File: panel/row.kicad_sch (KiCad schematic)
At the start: 16 parts

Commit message: Moving panel to subfolder
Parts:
- D? (x16): footprint ledcube:MHPA1515RGBDT -> panel:MHPA1515RGBDT
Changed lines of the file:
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@@
       (effects (font (size 1.27 1.27)) hide)
     )
-    (property "Footprint" "ledcube:MHPA1515RGBDT" (id 2) (at 114.3 58.42 0)
+    (property "Footprint" "panel:MHPA1515RGBDT" (id 2) (at 114.3 58.42 0)
       (effects (font (size 1.27 1.27)) hide)
     )
@@
       (effects (font (size 1.27 1.27)) hide)
     )
-    (property "Footprint" "ledcube:MHPA1515RGBDT" (id 2) (at 114.3 83.82 0)
+    (property "Footprint" "panel:MHPA1515RGBDT" (id 2) (at 114.3 83.82 0)
       (effects (font (size 1.27 1.27)) hide)
     )
@@
       (effects (font (size 1.27 1.27)) hide)
     )
-    (property "Footprint" "ledcube:MHPA1515RGBDT" (id 2) (at 114.3 109.22 0)
+    (property "Footprint" "panel:MHPA1515RGBDT" (id 2) (at 114.3 109.22 0)
       (effects (font (size 1.27 1.27)) hide)
     )
@@
       (effects (font (size 1.27 1.27)) hide)
     )
-    (property "Footprint" "ledcube:MHPA1515RGBDT" (id 2) (at 114.3 134.62 0)
+    (property "Footprint" "panel:MHPA1515RGBDT" (id 2) (at 114.3 134.62 0)
       (effects (font (size 1.27 1.27)) hide)
     )
@@
       (effects (font (size 1.27 1.27)) hide)
     )
-    (property "Footprint" "ledcube:MHPA1515RGBDT" (id 2) (at 135.89 58.42 0)
+    (property "Footprint" "panel:MHPA1515RGBDT" (id 2) (at 135.89 58.42 0)
       (effects (font (size 1.27 1.27)) hide)
     )
@@
       (effects (font (size 1.27 1.27)) hide)
     )
-    (property "Footprint" "ledcube:MHPA1515RGBDT" (id 2) (at 135.89 83.82 0)
+    (property "Footprint" "panel:MHPA1515RGBDT" (id 2) (at 135.89 83.82 0)
       (effects (font (size 1.27 1.27)) hide)
     )
@@
       (effects (font (size 1.27 1.27)) hide)
     )
-    (property "Footprint" "ledcube:MHPA1515RGBDT" (id 2) (at 135.89 109.22 0)
+    (property "Footprint" "panel:MHPA1515RGBDT" (id 2) (at 135.89 109.22 0)
       (effects (font (size 1.27 1.27)) hide)
     )
@@
       (effects (font (size 1.27 1.27)) hide)
     )
-    (property "Footprint" "ledcube:MHPA1515RGBDT" (id 2) (at 135.89 134.62 0)
+    (property "Footprint" "panel:MHPA1515RGBDT" (id 2) (at 135.89 134.62 0)
       (effects (font (size 1.27 1.27)) hide)
     )
@@
       (effects (font (size 1.27 1.27)) hide)
     )
-    (property "Footprint" "ledcube:MHPA1515RGBDT" (id 2) (at 157.48 58.42 0)
+    (property "Footprint" "panel:MHPA1515RGBDT" (id 2) (at 157.48 58.42 0)
       (effects (font (size 1.27 1.27)) hide)
     )
@@
       (effects (font (size 1.27 1.27)) hide)
     )
-    (property "Footprint" "ledcube:MHPA1515RGBDT" (id 2) (at 157.48 83.82 0)
+    (property "Footprint" "panel:MHPA1515RGBDT" (id 2) (at 157.48 83.82 0)
       (effects (font (size 1.27 1.27)) hide)
     )
@@
       (effects (font (size 1.27 1.27)) hide)
     )
-    (property "Footprint" "ledcube:MHPA1515RGBDT" (id 2) (at 157.48 109.22 0)
+    (property "Footprint" "panel:MHPA1515RGBDT" (id 2) (at 157.48 109.22 0)
       (effects (font (size 1.27 1.27)) hide)
     )
@@
       (effects (font (size 1.27 1.27)) hide)
     )
-    (property "Footprint" "ledcube:MHPA1515RGBDT" (id 2) (at 157.48 134.62 0)
+    (property "Footprint" "panel:MHPA1515RGBDT" (id 2) (at 157.48 134.62 0)
       (effects (font (size 1.27 1.27)) hide)
     )
@@
       (effects (font (size 1.27 1.27)) hide)
     )
-    (property "Footprint" "ledcube:MHPA1515RGBDT" (id 2) (at 179.07 58.42 0)
+    (property "Footprint" "panel:MHPA1515RGBDT" (id 2) (at 179.07 58.42 0)
       (effects (font (size 1.27 1.27)) hide)
     )
@@
       (effects (font (size 1.27 1.27)) hide)
     )
-    (property "Footprint" "ledcube:MHPA1515RGBDT" (id 2) (at 179.07 83.82 0)
+    (property "Footprint" "panel:MHPA1515RGBDT" (id 2) (at 179.07 83.82 0)
       (effects (font (size 1.27 1.27)) hide)
     )
@@
       (effects (font (size 1.27 1.27)) hide)
     )
-    (property "Footprint" "ledcube:MHPA1515RGBDT" (id 2) (at 179.07 109.22 0)
+    (property "Footprint" "panel:MHPA1515RGBDT" (id 2) (at 179.07 109.22 0)
       (effects (font (size 1.27 1.27)) hide)
     )
@@
       (effects (font (size 1.27 1.27)) hide)
     )
-    (property "Footprint" "ledcube:MHPA1515RGBDT" (id 2) (at 179.07 134.62 0)
-      (effects (font (size 1.27 1.27)) hide)
-    )
+    (property "Footprint" "panel:MHPA1515RGBDT" (id 2) (at 179.07 134.62 0)
+      (effects (font (size 1.27 1.27)) hide)
+    )

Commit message: Annotated schematic
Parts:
- removed D? (x15): LED_RABG, panel:MHPA1515RGBDT, symbol Device:LED_RABG
- added D242, D243, D244, D245, D246, D247, D248, D249, D250, D251, D252, D253, D254, D255, D256: LED_RABG, panel:MHPA1515RGBDT, symbol Device:LED_RABG
- gave numbers to parts that had none: 1
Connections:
- net COL_10B: now also D251.3 (BK)
- net COL_10G: now also D251.4 (GK)
- net COL_10R: now also D251.1 (RK)
- net COL_11B: now also D255.3 (BK)
- net COL_11G: now also D255.4 (GK)
- net COL_11R: now also D255.1 (RK)
- net COL_12B: now also D244.3 (BK)
- net COL_12G: now also D244.4 (GK)
- net COL_12R: now also D244.1 (RK)
- net COL_13B: now also D248.3 (BK)
- net COL_13G: now also D248.4 (GK)
- net COL_13R: now also D248.1 (RK)
- net COL_14B: now also D252.3 (BK)
- net COL_14G: now also D252.4 (GK)
- net COL_14R: now also D252.1 (RK)
- net COL_15B: now also D256.3 (BK)
- net COL_15G: now also D256.4 (GK)
- net COL_15R: now also D256.1 (RK)
- net COL_1B: now also D245.3 (BK)
- net COL_1G: now also D245.4 (GK)
- net COL_1R: now also D245.1 (RK)
- net COL_2B: now also D249.3 (BK)
- net COL_2G: now also D249.4 (GK)
- net COL_2R: now also D249.1 (RK)
- net COL_3B: now also D253.3 (BK)
- net COL_3G: now also D253.4 (GK)
- net COL_3R: now also D253.1 (RK)
- net COL_4B: now also D242.3 (BK)
- net COL_4G: now also D242.4 (GK)
- net COL_4R: now also D242.1 (RK)
- net COL_5B: now also D246.3 (BK)
- net COL_5G: now also D246.4 (GK)
- net COL_5R: now also D246.1 (RK)
- net COL_6B: now also D250.3 (BK)
- net COL_6G: now also D250.4 (GK)
- net COL_6R: now also D250.1 (RK)
- net COL_7B: now also D254.3 (BK)
- net COL_7G: now also D254.4 (GK)
- net COL_7R: now also D254.1 (RK)
- net COL_8B: now also D243.3 (BK)
- net COL_8G: now also D243.4 (GK)
- net COL_8R: now also D243.1 (RK)
- net COL_9B: now also D247.3 (BK)
- net COL_9G: now also D247.4 (GK)
- net COL_9R: now also D247.1 (RK)
- net COMMON: now also D242.2 (A), D243.2 (A), D244.2 (A), D245.2 (A), D246.2 (A), D247.2 (A), D248.2 (A), D249.2 (A), D250.2 (A), D251.2 (A), D252.2 (A), D253.2 (A), D254.2 (A), D255.2 (A), D256.2 (A)
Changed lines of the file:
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@@
   (symbol (lib_id "Device:LED_RABG") (at 113.03 58.42 90)
     (in_bom yes) (on_board yes)
-    (property "Reference" "D?" (id 0) (at 106.172 53.34 90))
+    (property "Reference" "D241" (id 0) (at 106.172 53.34 90))
     (property "Value" "LED_RABG" (id 1) (at 121.92 58.42 0)
       (effects (font (size 1.27 1.27)) hide)
@@
   (symbol (lib_id "Device:LED_RABG") (at 113.03 83.82 90)
     (in_bom yes) (on_board yes)
-    (property "Reference" "D?" (id 0) (at 106.172 78.74 90))
+    (property "Reference" "D242" (id 0) (at 106.172 78.74 90))
     (property "Value" "LED_RABG" (id 1) (at 121.92 83.82 0)
       (effects (font (size 1.27 1.27)) hide)
@@
   (symbol (lib_id "Device:LED_RABG") (at 113.03 109.22 90)
     (in_bom yes) (on_board yes)
-    (property "Reference" "D?" (id 0) (at 106.172 104.14 90))
+    (property "Reference" "D243" (id 0) (at 106.172 104.14 90))
     (property "Value" "LED_RABG" (id 1) (at 121.92 109.22 0)
       (effects (font (size 1.27 1.27)) hide)
@@
   (symbol (lib_id "Device:LED_RABG") (at 113.03 134.62 90)
     (in_bom yes) (on_board yes)
-    (property "Reference" "D?" (id 0) (at 106.172 129.54 90))
+    (property "Reference" "D244" (id 0) (at 106.172 129.54 90))
     (property "Value" "LED_RABG" (id 1) (at 121.92 134.62 0)
       (effects (font (size 1.27 1.27)) hide)
@@
   (symbol (lib_id "Device:LED_RABG") (at 134.62 58.42 90)
     (in_bom yes) (on_board yes)
-    (property "Reference" "D?" (id 0) (at 127.762 53.34 90))
+    (property "Reference" "D245" (id 0) (at 127.762 53.34 90))
     (property "Value" "LED_RABG" (id 1) (at 143.51 58.42 0)
       (effects (font (size 1.27 1.27)) hide)
@@
   (symbol (lib_id "Device:LED_RABG") (at 134.62 83.82 90)
     (in_bom yes) (on_board yes)
-    (property "Reference" "D?" (id 0) (at 127.762 78.74 90))
+    (property "Reference" "D246" (id 0) (at 127.762 78.74 90))
     (property "Value" "LED_RABG" (id 1) (at 143.51 83.82 0)
       (effects (font (size 1.27 1.27)) hide)
@@
   (symbol (lib_id "Device:LED_RABG") (at 134.62 109.22 90)
     (in_bom yes) (on_board yes)
-    (property "Reference" "D?" (id 0) (at 127.762 104.14 90))
+    (property "Reference" "D247" (id 0) (at 127.762 104.14 90))
     (property "Value" "LED_RABG" (id 1) (at 143.51 109.22 0)
       (effects (font (size 1.27 1.27)) hide)
@@
   (symbol (lib_id "Device:LED_RABG") (at 134.62 134.62 90)
     (in_bom yes) (on_board yes)
-    (property "Reference" "D?" (id 0) (at 127.762 129.54 90))
+    (property "Reference" "D248" (id 0) (at 127.762 129.54 90))
     (property "Value" "LED_RABG" (id 1) (at 143.51 134.62 0)
       (effects (font (size 1.27 1.27)) hide)
@@
   (symbol (lib_id "Device:LED_RABG") (at 156.21 58.42 90)
     (in_bom yes) (on_board yes)
-    (property "Reference" "D?" (id 0) (at 149.352 53.34 90))
+    (property "Reference" "D249" (id 0) (at 149.352 53.34 90))
     (property "Value" "LED_RABG" (id 1) (at 165.1 58.42 0)
       (effects (font (size 1.27 1.27)) hide)
@@
   (symbol (lib_id "Device:LED_RABG") (at 156.21 83.82 90)
     (in_bom yes) (on_board yes)
-    (property "Reference" "D?" (id 0) (at 149.352 78.74 90))
+    (property "Reference" "D250" (id 0) (at 149.352 78.74 90))
     (property "Value" "LED_RABG" (id 1) (at 165.1 83.82 0)
       (effects (font (size 1.27 1.27)) hide)
@@
   (symbol (lib_id "Device:LED_RABG") (at 156.21 109.22 90)
     (in_bom yes) (on_board yes)
-    (property "Reference" "D?" (id 0) (at 149.352 104.14 90))
+    (property "Reference" "D251" (id 0) (at 149.352 104.14 90))
     (property "Value" "LED_RABG" (id 1) (at 165.1 109.22 0)
       (effects (font (size 1.27 1.27)) hide)
@@
   (symbol (lib_id "Device:LED_RABG") (at 156.21 134.62 90)
     (in_bom yes) (on_board yes)
-    (property "Reference" "D?" (id 0) (at 149.352 129.54 90))
+    (property "Reference" "D252" (id 0) (at 149.352 129.54 90))
     (property "Value" "LED_RABG" (id 1) (at 165.1 134.62 0)
       (effects (font (size 1.27 1.27)) hide)
@@
   (symbol (lib_id "Device:LED_RABG") (at 177.8 58.42 90)
     (in_bom yes) (on_board yes)
-    (property "Reference" "D?" (id 0) (at 170.942 53.34 90))
+    (property "Reference" "D253" (id 0) (at 170.942 53.34 90))
     (property "Value" "LED_RABG" (id 1) (at 186.69 58.42 0)
       (effects (font (size 1.27 1.27)) hide)
@@
   (symbol (lib_id "Device:LED_RABG") (at 177.8 83.82 90)
     (in_bom yes) (on_board yes)
-    (property "Reference" "D?" (id 0) (at 170.942 78.74 90))
+    (property "Reference" "D254" (id 0) (at 170.942 78.74 90))
     (property "Value" "LED_RABG" (id 1) (at 186.69 83.82 0)
       (effects (font (size 1.27 1.27)) hide)
@@
   (symbol (lib_id "Device:LED_RABG") (at 177.8 109.22 90)
     (in_bom yes) (on_board yes)
-    (property "Reference" "D?" (id 0) (at 170.942 104.14 90))
+    (property "Reference" "D255" (id 0) (at 170.942 104.14 90))
     (property "Value" "LED_RABG" (id 1) (at 186.69 109.22 0)
       (effects (font (size 1.27 1.27)) hide)
@@
   (symbol (lib_id "Device:LED_RABG") (at 177.8 134.62 90)
     (in_bom yes) (on_board yes)
-    (property "Reference" "D?" (id 0) (at 170.942 129.54 90))
+    (property "Reference" "D256" (id 0) (at 170.942 129.54 90))
     (property "Value" "LED_RABG" (id 1) (at 186.69 134.62 0)
       (effects (font (size 1.27 1.27)) hide)

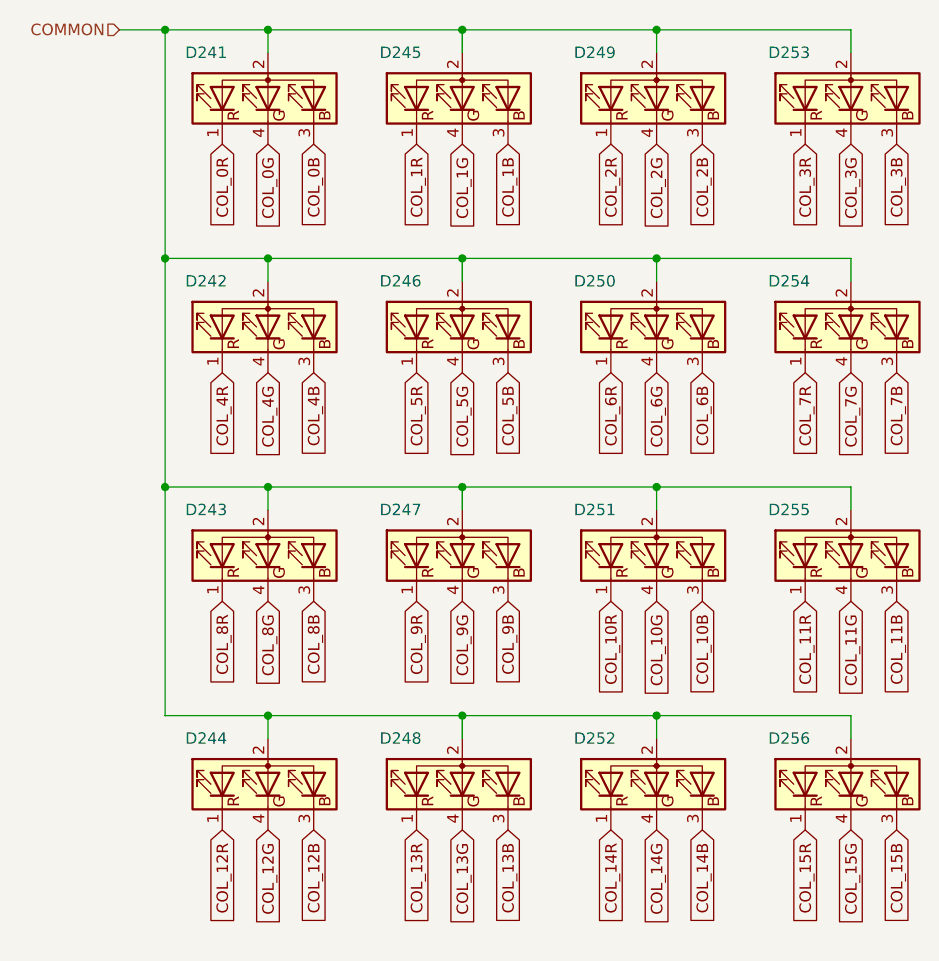
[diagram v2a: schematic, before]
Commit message: LED matrix placement
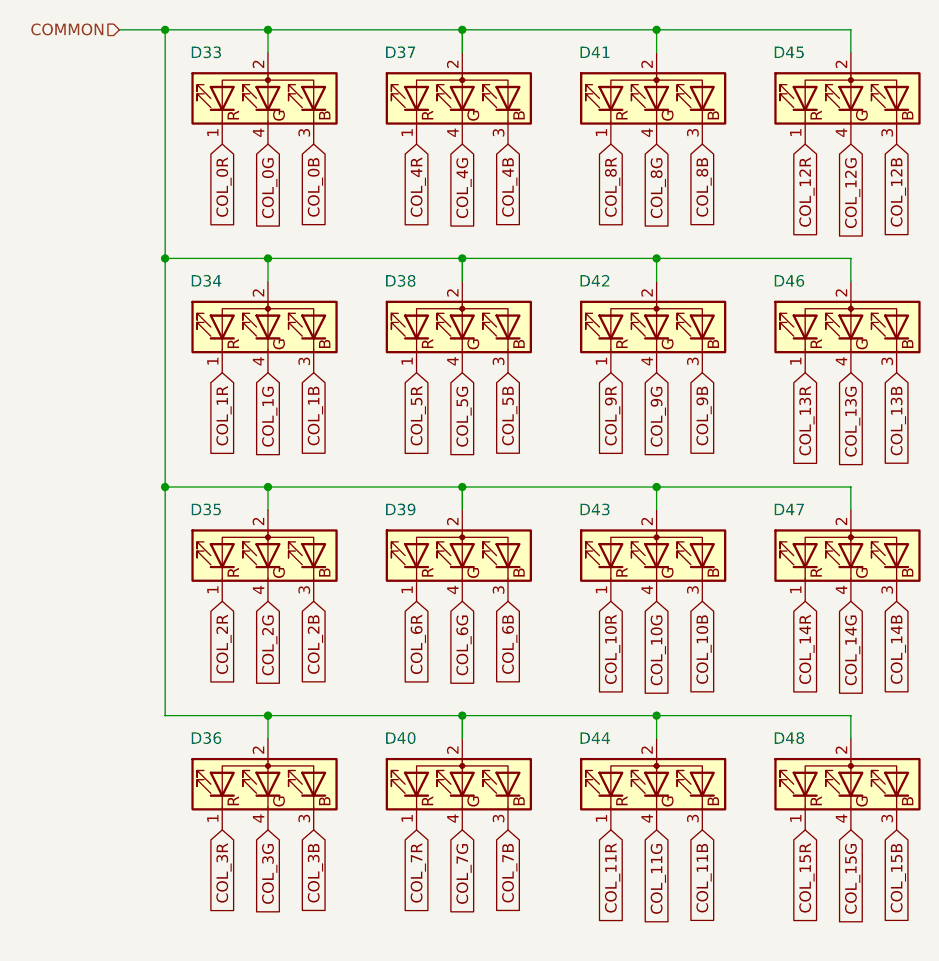
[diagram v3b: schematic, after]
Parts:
- renumbered D241 to D33, D242 to D34, D243 to D35, D244 to D36, D245 to D37, D246 to D38, D247 to D39, D248 to D40, D249 to D41, D250 to D42, D251 to D43, D252 to D44, D253 to D45, D254 to D46, D255 to D47, D256 to D48
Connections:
- net COL_11B: now also D44.3 (BK); no longer D47.3 (BK)
- net COL_11G: now also D44.4 (GK); no longer D47.4 (GK)
- net COL_11R: now also D44.1 (RK); no longer D47.1 (RK)
- net COL_12B: now also D45.3 (BK); no longer D36.3 (BK)
- net COL_12G: now also D45.4 (GK); no longer D36.4 (GK)
- net COL_12R: now also D45.1 (RK); no longer D36.1 (RK)
- net COL_13B: now also D46.3 (BK); no longer D40.3 (BK)
- net COL_13G: now also D46.4 (GK); no longer D40.4 (GK)
- net COL_13R: now also D46.1 (RK); no longer D40.1 (RK)
- net COL_14B: now also D47.3 (BK); no longer D44.3 (BK)
- net COL_14G: now also D47.4 (GK); no longer D44.4 (GK)
- net COL_14R: now also D47.1 (RK); no longer D44.1 (RK)
- net COL_1B: now also D34.3 (BK); no longer D37.3 (BK)
- net COL_1G: now also D34.4 (GK); no longer D37.4 (GK)
- net COL_1R: now also D34.1 (RK); no longer D37.1 (RK)
- net COL_2B: now also D35.3 (BK); no longer D41.3 (BK)
- net COL_2G: now also D35.4 (GK); no longer D41.4 (GK)
- net COL_2R: now also D35.1 (RK); no longer D41.1 (RK)
- net COL_3B: now also D36.3 (BK); no longer D45.3 (BK)
- net COL_3G: now also D36.4 (GK); no longer D45.4 (GK)
- net COL_3R: now also D36.1 (RK); no longer D45.1 (RK)
- net COL_4B: now also D37.3 (BK); no longer D34.3 (BK)
- net COL_4G: now also D37.4 (GK); no longer D34.4 (GK)
- net COL_4R: now also D37.1 (RK); no longer D34.1 (RK)
- net COL_6B: now also D39.3 (BK); no longer D42.3 (BK)
- net COL_6G: now also D39.4 (GK); no longer D42.4 (GK)
- net COL_6R: now also D39.1 (RK); no longer D42.1 (RK)
- net COL_7B: now also D40.3 (BK); no longer D46.3 (BK)
- net COL_7G: now also D40.4 (GK); no longer D46.4 (GK)
- net COL_7R: now also D40.1 (RK); no longer D46.1 (RK)
- net COL_8B: now also D41.3 (BK); no longer D35.3 (BK)
- net COL_8G: now also D41.4 (GK); no longer D35.4 (GK)
- net COL_8R: now also D41.1 (RK); no longer D35.1 (RK)
- net COL_9B: now also D42.3 (BK); no longer D39.3 (BK)
- net COL_9G: now also D42.4 (GK); no longer D39.4 (GK)
- net COL_9R: now also D42.1 (RK); no longer D39.1 (RK)
